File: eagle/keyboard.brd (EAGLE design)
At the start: 160 x 100 mm, 71 parts, among them Q1 12MHz

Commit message: Fix up schematic and finish placing the buttons in the keyboard brd
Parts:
- removed JOYSTICK: (no value), pinhead:1_05X2MM
- removed PROG1: (no value), pinhead:1X04
- added J2: (no value), pinhead:1X04
- added J3: (no value), pinhead:1X05
- moved S60 251.1 mm to (155.0, 6.00), turned to 90 degrees
- moved S29 235.4 mm to (145.0, 36.0), turned to 90 degrees
- moved S20 233.9 mm to (155.0, 46.0), turned to 90 degrees
- moved S59 232.5 mm to (145.0, 6.00), turned to 90 degrees
- moved S50 225.5 mm to (155.0, 16.0), turned to 90 degrees
- moved S37 218.6 mm to (125.0, 26.0), turned to 90 degrees
- moved S28 215.3 mm to (135.0, 36.0), turned to 90 degrees
- moved S58 214.1 mm to (135.0, 6.00), turned to 90 degrees
- moved S10 213.7 mm to (155.0, 56.0), turned to 90 degrees
- moved S19 213.7 mm to (145.0, 46.0), turned to 90 degrees
- moved S49 206.6 mm to (145.0, 16.0), turned to 90 degrees
- moved S45 204.2 mm to (105.0, 16.0), turned to 90 degrees
- moved S5 203.3 mm to (105.0, 56.0), turned to 90 degrees
- moved S40 200.5 mm to (155.0, 26.0), turned to 90 degrees
- moved S36 198.9 mm to (115.0, 26.0), turned to 90 degrees
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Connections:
- net BTN: now also J3.5; no longer JOYSTICK.5
- net GND: now also J2.2, J3.1; no longer JOYSTICK.1, PROG1.2
- net RXD/COL3: now also J2.3; no longer PROG1.3
- net TXD/COL4: now also J2.4; no longer PROG1.4
- net VCC: now also J2.1, J3.2; no longer JOYSTICK.2, PROG1.1
- net XAXIS: now also J3.3; no longer JOYSTICK.3
- net YAXIS: now also J3.4; no longer JOYSTICK.4
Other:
- board size 160 x 100 mm -> 100 x 100 mm

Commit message: Add joystick support in keyboard schematic
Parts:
- added J4: (no value), pinhead:1X07
- moved J3 176.3 mm to (124.0, 77.0), flipped to the bottom, turned to 270 degrees
- moved U$1 87.5 mm to (45.1, 75.3)

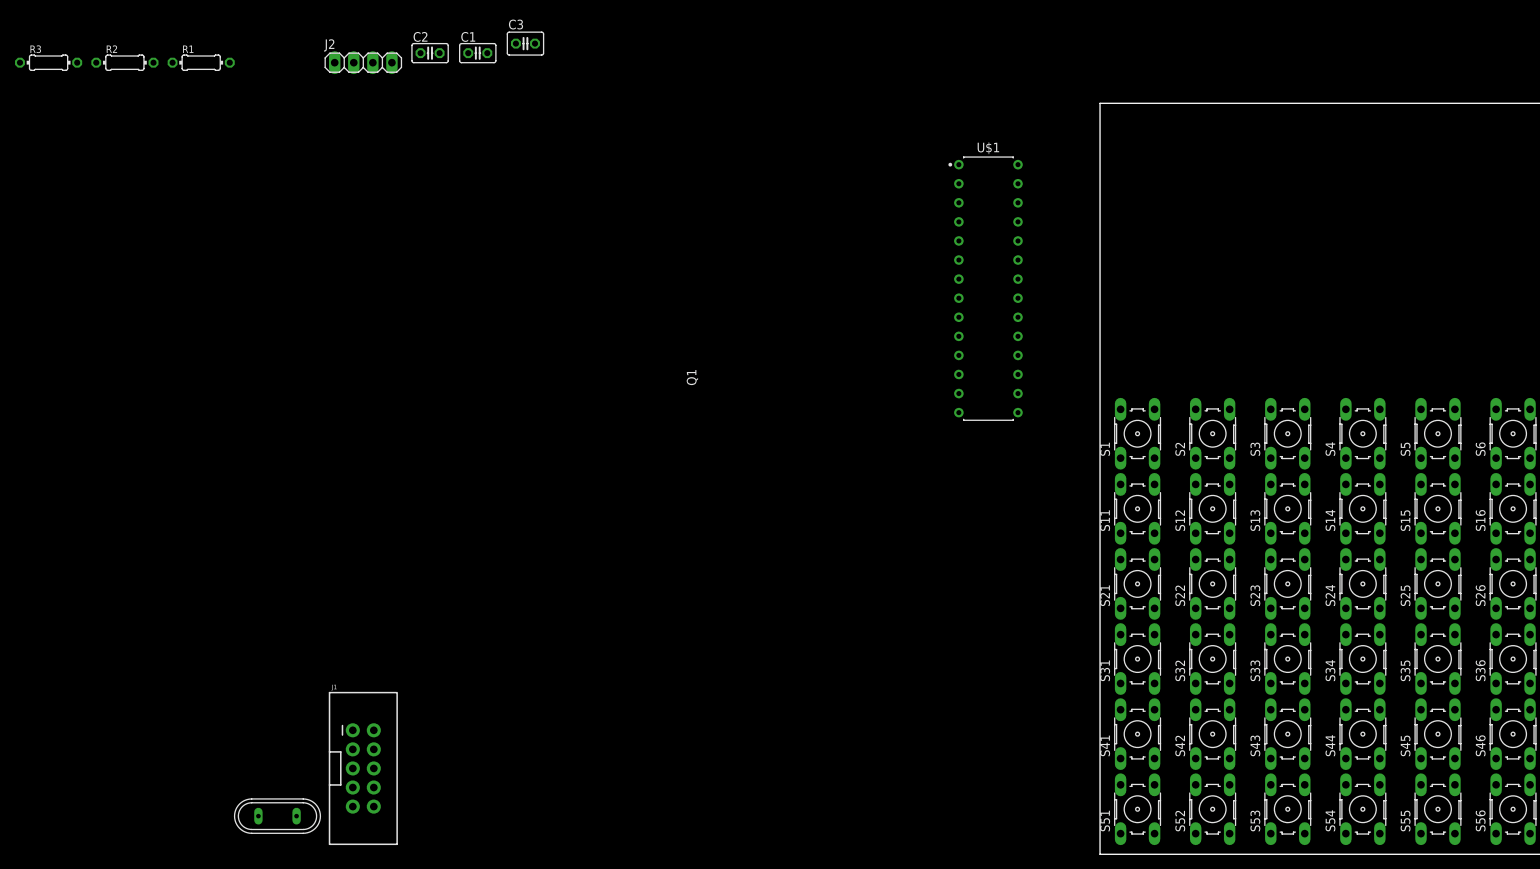
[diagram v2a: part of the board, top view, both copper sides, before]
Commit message: Finish placing components
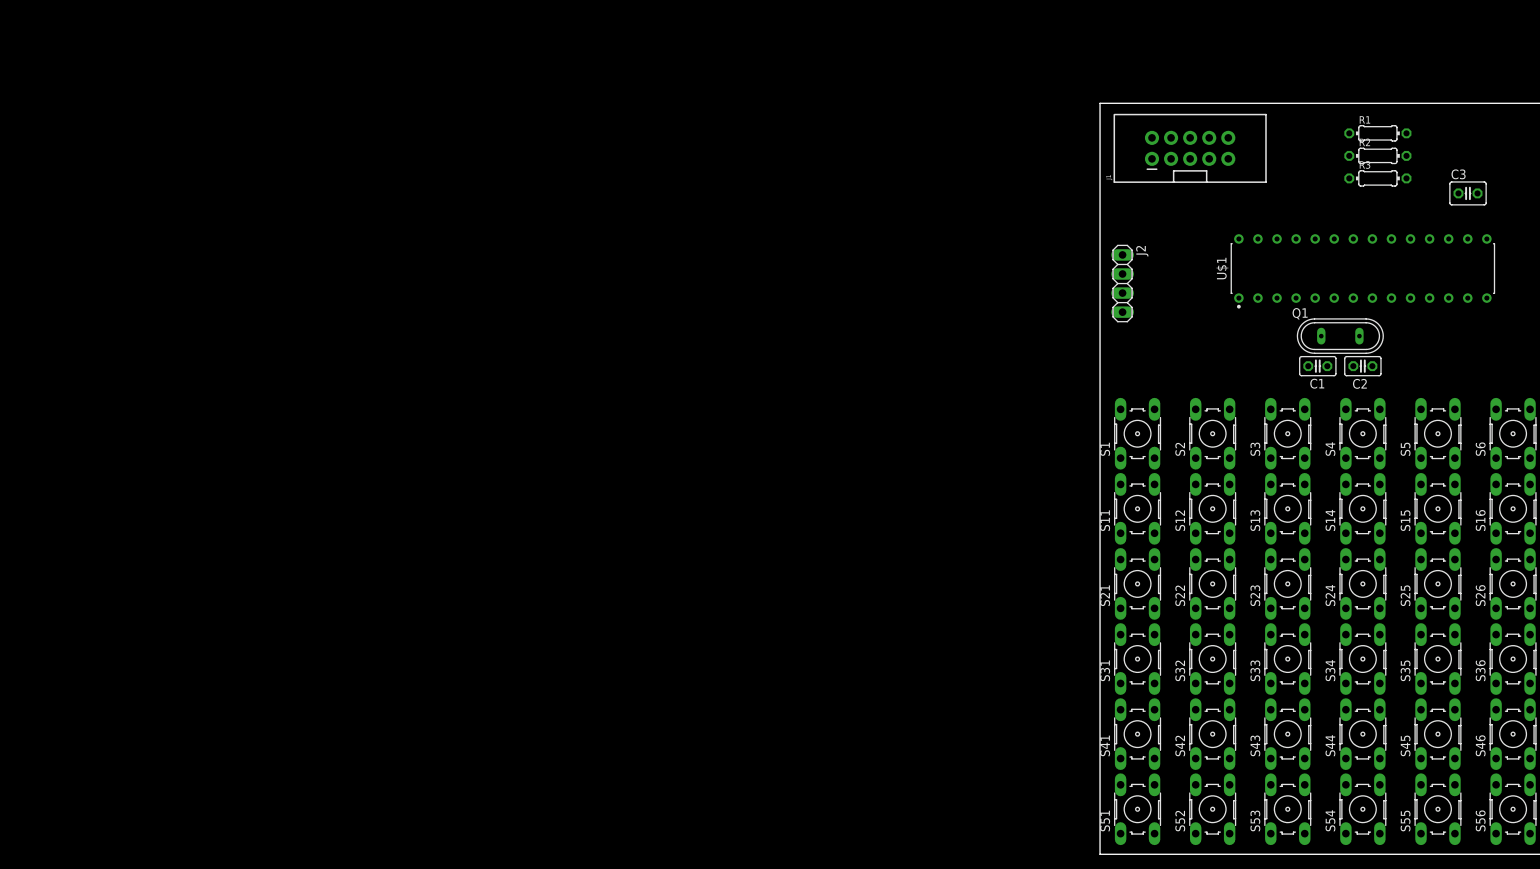
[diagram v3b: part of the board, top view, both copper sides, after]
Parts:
- moved R3 177.7 mm to (97.0, 90.0)
- moved R2 167.3 mm to (97.0, 93.0)
- moved R1 157.0 mm to (97.0, 96.0)
- moved Q1 155.3 mm to (92.0, 69.0)
- moved J1 137.6 mm to (72.0, 94.0), turned to 90 degrees
- moved C2 131.0 mm to (95.0, 65.0), turned to 180 degrees
- moved C3 127.1 mm to (109.0, 88.0)
- moved C1 119.4 mm to (89.0, 65.0), turned to 180 degrees
- moved J2 105.3 mm to (63.0, 76.0), turned to 270 degrees
- moved U$1 49.9 mm to (95.0, 78.0), turned to 90 degrees
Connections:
- net XTAL1: now also C2.2, Q1.2; no longer C1.2, Q1.1
- net XTAL2: now also C1.2, Q1.1; no longer C2.2, Q1.2

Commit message: Fix schematic button matrix
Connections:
- removed net N$1: S1.2, S11.1
- removed net N$10: S42.2, S52.1
- removed net N$11: S13.1, S3.2
- removed net N$12: S13.2, S23.1
- removed net N$13: S23.2, S33.1
- removed net N$14: S33.2, S43.1
- removed net N$15: S43.2, S53.1
- removed net N$16: S14.1, S4.2
- removed net N$17: S14.2, S24.1
- removed net N$18: S24.2, S34.1
- removed net N$19: S34.2, S44.1
- removed net N$2: S11.2, S21.1
- removed net N$20: S44.2, S54.1
- removed net N$21: S15.1, S5.2
- removed net N$22: S15.2, S25.1
- removed net N$23: S25.2, S35.1
- removed net N$24: S35.2, S45.1
- removed net N$25: S45.2, S55.1
- removed net N$26: S16.1, S6.2
- removed net N$27: S16.2, S26.1
- removed net N$28: S26.2, S36.1
- removed net N$29: S36.2, S46.1
- removed net N$3: S21.2, S31.1
- removed net N$30: S46.2, S56.1
- removed net N$31: S17.1, S7.2
- removed net N$32: S17.2, S27.1
- removed net N$33: S27.2, S37.1
- removed net N$34: S37.2, S47.1
- removed net N$35: S47.2, S57.1
- removed net N$36: S18.1, S8.2
- removed net N$37: S18.2, S28.1
- removed net N$38: S28.2, S38.1
- removed net N$39: S38.2, S48.1
- removed net N$4: S31.2, S41.1
- removed net N$40: S48.2, S58.1
- removed net N$41: S49.2, S59.1
- removed net N$42: S29.2, S39.1
- removed net N$43: S19.2, S29.1
- removed net N$44: S19.1, S9.2
- removed net N$45: S10.2, S20.1
- removed net N$46: S20.2, S30.1
- removed net N$47: S30.2, S40.1
- removed net N$48: S40.2, S50.1
- removed net N$49: S39.2, S49.1
- removed net N$5: S41.2, S51.1
- removed net N$50: S50.2, S60.1
- removed net N$6: S12.1, S2.2
- removed net N$7: S12.2, S22.1
- removed net N$8: S22.2, S32.1
- removed net N$9: S32.2, S42.1
- net COL1: now also S1.1, S1.2, S11.1, S11.2, S21.1, S21.2, S31.1, S31.2, S41.1, S41.2, S51.1
- net COL10: now also S10.1, S10.2, S20.1, S20.2, S30.1, S30.2, S40.1, S40.2, S50.1, S50.2, S60.1
- net COL2: now also S12.1, S12.2, S2.1, S2.2, S22.1, S22.2, S32.1, S32.2, S42.1, S42.2, S52.1
- net COL5: now also S15.1, S15.2, S25.1, S25.2, S35.1, S35.2, S45.1, S45.2, S5.1, S5.2, S55.1
- net COL6: now also S16.1, S16.2, S26.1, S26.2, S36.1, S36.2, S46.1, S46.2, S56.1, S6.1, S6.2
- net COL7: now also S17.1, S17.2, S27.1, S27.2, S37.1, S37.2, S47.1, S47.2, S57.1, S7.1, S7.2
- net COL8: now also S18.1, S18.2, S28.1, S28.2, S38.1, S38.2, S48.1, S48.2, S58.1, S8.1, S8.2
- net COL9: now also S19.1, S19.2, S29.1, S29.2, S39.1, S39.2, S49.1, S49.2, S59.1, S9.1, S9.2
- net RXD/COL3: now also S13.1, S13.2, S23.1, S23.2, S3.1, S3.2, S33.1, S33.2, S43.1, S43.2, S53.1
- net TXD/COL4: now also S14.1, S14.2, S24.1, S24.2, S34.1, S34.2, S4.1, S4.2, S44.1, S44.2, S54.1

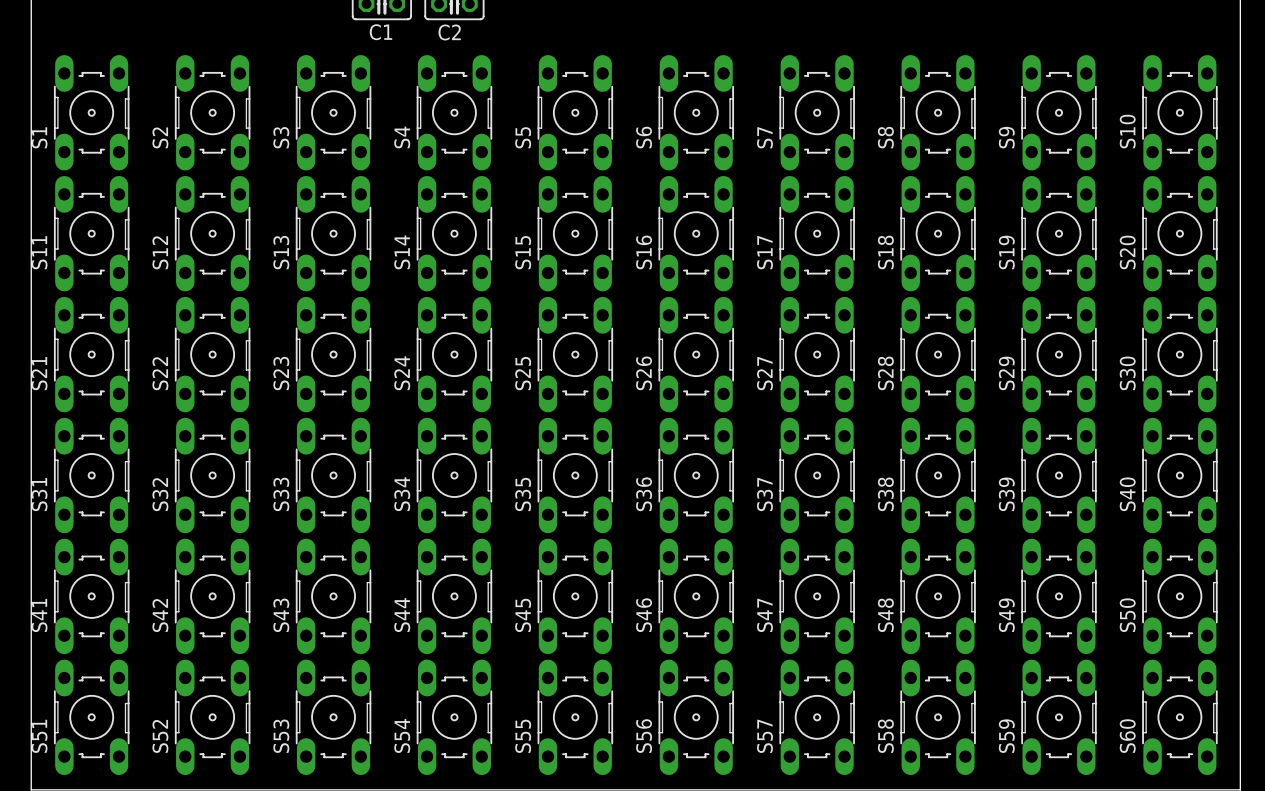
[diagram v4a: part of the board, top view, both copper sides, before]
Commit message: Add most keyboard wires
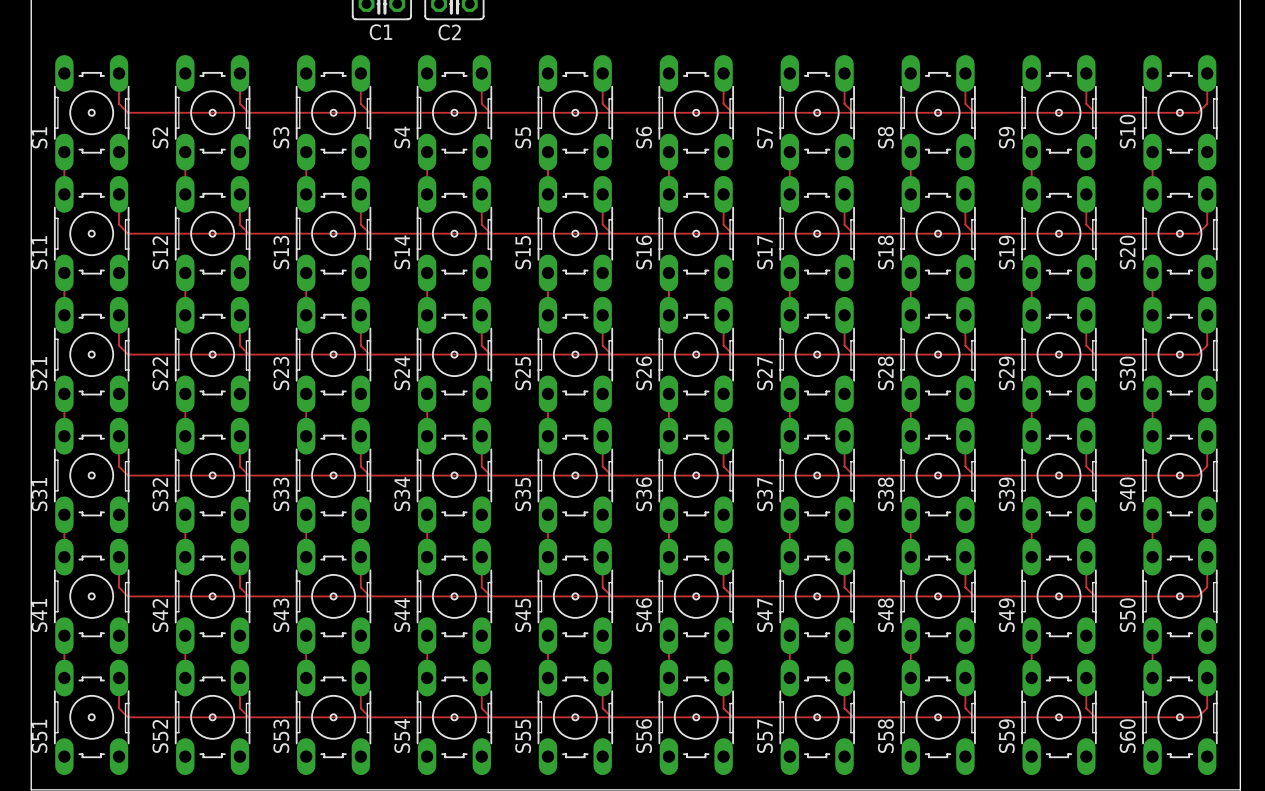
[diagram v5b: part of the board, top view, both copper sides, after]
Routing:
- net ROW5: track 0.00 -> 124.1 mm
- net ROW4: track 0.00 -> 124.1 mm
- net ROW6: track 0.00 -> 124.1 mm
- net ROW3: track 0.00 -> 124.1 mm
- net ROW2: track 0.00 -> 124.1 mm
- net ROW1: track 0.00 -> 124.1 mm
- net TXD/COL4: track 0.00 -> 17.5 mm
- net RXD/COL3: track 0.00 -> 17.5 mm
- net COL9: track 0.00 -> 17.5 mm
- net COL8: track 0.00 -> 17.5 mm
- net COL7: track 0.00 -> 17.5 mm
- net COL6: track 0.00 -> 17.5 mm
- net COL5: track 0.00 -> 17.5 mm
- net COL2: track 0.00 -> 17.5 mm
- net COL10: track 0.00 -> 17.5 mm
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
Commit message: Finish most of front side of board
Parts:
- moved C3 38.9 mm to (70.5, 82.5), turned to 270 degrees
- moved R1 8.38 mm to (89.0, 93.5), turned to 90 degrees
- moved R2 5.02 mm to (92.0, 93.5), turned to 90 degrees
- moved R3 4.03 mm to (95.0, 93.5), turned to 90 degrees
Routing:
- net VCC: track 0.00 -> 98.0 mm
- net COL10: track 17.5 -> 70.9 mm
- net COL9: track 17.5 -> 64.0 mm
- net COL8: track 17.5 -> 57.1 mm
- net YAXIS: track 0.00 -> 38.9 mm
- net COL7: track 17.5 -> 50.2 mm
- net SBDI_EN: track 0.00 -> 31.9 mm
- net SBDI_DAT: track 0.00 -> 31.1 mm
- net BTN: track 0.00 -> 30.2 mm
- net SBDI_CLK: track 0.00 -> 29.6 mm
- net XAXIS: track 0.00 -> 29.3 mm
- net COL6: track 17.5 -> 43.3 mm
- net COL1: track 17.5 -> 40.9 mm
- net TXD/COL4: track 17.5 -> 40.3 mm
- net COL2: track 17.5 -> 35.7 mm
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- added copper zone on layer 1, net GND

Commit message: Finish basic board design
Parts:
- IC1: value STC12C5616AD-28PIN -> STC12C5616AD
- moved C3 7.38 mm to (77.0, 86.0), turned to 0 degrees
- moved J2 4.00 mm to (63.0, 72.0)
- renumbered U$1 to IC1
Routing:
- net ROW6: track 124.1 -> 199.4 mm
- net ROW5: track 124.1 -> 195.4 mm
- net ROW4: track 124.1 -> 191.7 mm
- net RXD/COL3: track 33.7 -> 95.3 mm, vias 0 -> 2
- net TXD/COL4: track 40.3 -> 101.8 mm, vias 0 -> 2
- net ROW3: track 124.1 -> 172.5 mm
- net ROW2: track 124.1 -> 169.8 mm
- net COL5: track 35.0 -> 74.0 mm
- net COL7: track 50.2 -> 89.2 mm
- net COL2: track 35.7 -> 74.7 mm
- net COL1: track 40.9 -> 79.9 mm
- net COL8: track 57.1 -> 96.1 mm
- net COL6: track 43.3 -> 82.4 mm
- net COL10: track 70.9 -> 109.9 mm
- net COL9: track 64.0 -> 103.0 mm
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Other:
- board text added: "GND"
- board text added: "Keyboard Programming Header"
- board text added: "RXD"
- board text added: "TXD"
- board text added: "VCC"
